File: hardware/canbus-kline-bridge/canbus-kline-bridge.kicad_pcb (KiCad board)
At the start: 4 copper layers, 55 x 35 mm, 38 parts, among them J1 USB_B_Micro, J2 SWD, J4 CANBus, J5 CANBus, J6 K-Line, Q1 2N7002, Q2 2N7002, U1 MCP1754S-3302xCB, U2 STM32F042F6Px, U3 Voltage Regulator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

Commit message: Working on the kline bridge a bit more
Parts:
- removed JP1: CAN_RX/USB_D-, Connector_PinHeader_2.54mm:PinHeader_1x03_P2.54mm_Vertical
- removed JP2: CAN_TX/USB_D+, Connector_PinHeader_2.54mm:PinHeader_1x03_P2.54mm_Vertical
- added R5: 10k, Resistor_SMD:R_0805_2012Metric_Pad1.20x1.40mm_HandSolder, B.Cu at (84.7, 93.2)
- added R6: 10k, Resistor_SMD:R_0805_2012Metric_Pad1.20x1.40mm_HandSolder, B.Cu at (88.1, 91.4)
- added R7: 10k, Resistor_SMD:R_0805_2012Metric_Pad1.20x1.40mm_HandSolder, B.Cu at (75.9, 92.6)
- added R8: 10k, Resistor_SMD:R_0805_2012Metric_Pad1.20x1.40mm_HandSolder, B.Cu at (73.6, 97.0)
- added U6: CY15E004J, Package_SO:SOIC-8_5.23x5.23mm_P1.27mm, B.Cu at (91.6, 86.2)
- added U7: MCP2517FD, Package_SO:SOIC-14_3.9x8.7mm_P1.27mm, F.Cu at (76.0, 96.0)
- added X1: ASV-20.000MHZ-EJ-T, Oscillator:Oscillator_SMD_Abracon_ASV-4Pin_7.0x5.1mm, B.Cu at (68.9, 99.3)
- R3: moved to B.Cu
- moved R1 6.15 mm to (93.0, 96.4), turned to 0 degrees
- moved R2 4.75 mm to (99.9, 93.1)
- moved R3 0.08 mm to (77.4, 87.6)
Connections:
- S1 pad 2: unconnected-(S1-Pad2) -> +3V3
- S1 pad 4: unconnected-(S1-Pad4) -> /Net-(R1-Pad1)
- S2 pad 2: unconnected-(S2-Pad2) -> GND
- S2 pad 4: unconnected-(S2-Pad4) -> ~{RESET}
- U2 pad 10: unconnected-(U2-Pad10) -> ~{SPI_SS}
- U2 pad 11: unconnected-(U2-Pad11) -> SCK
- U2 pad 12: unconnected-(U2-Pad12) -> MISO
- U2 pad 13: unconnected-(U2-Pad13) -> MOSI
- U2 pad 17: Net-(JP1-Pad2) -> USB_D-
- U2 pad 18: Net-(JP2-Pad2) -> USB_D+
- U2 pad 2: SDA1 -> SDA
- U2 pad 3: SCL1 -> SCL
- U2 pad 7: unconnected-(U2-Pad7) -> ~{CAN_INT}
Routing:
- net ~{CAN_INT}: track 0.00 -> 25.5 mm, vias 0 -> 2
- net SCK: track 0.00 -> 18.4 mm, vias 0 -> 2
- net ~{SPI_SS}: track 0.00 -> 18.4 mm, vias 0 -> 2
- net +3V3: track 23.1 -> 40.3 mm, vias 5 -> 11
- net MISO: track 0.00 -> 16.6 mm, vias 0 -> 2
- net MOSI: track 0.00 -> 16.0 mm, vias 0 -> 2
- net Net-(JP1-Pad2): track 13.1 -> 0.00 mm, vias 1 -> 0
- net SCL: track 0.00 -> 9.90 mm, vias 0 -> 2
- net SDA: track 0.00 -> 9.40 mm, vias 0 -> 2
- net USB_D-: track 17.0 -> 25.3 mm, vias 1 -> 2
- net GND: track 18.7 -> 26.6 mm, vias 6 -> 7
- net Net-(JP2-Pad2): track 7.63 -> 0.00 mm, vias 1 -> 0
- net CAN_TX: track 12.5 -> 6.76 mm, vias 1 -> 2
- net Net-(U7-Pad6): track 0.00 -> 4.83 mm, vias 0 -> 1
- net K_LINE_EN: track 17.1 -> 12.8 mm
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
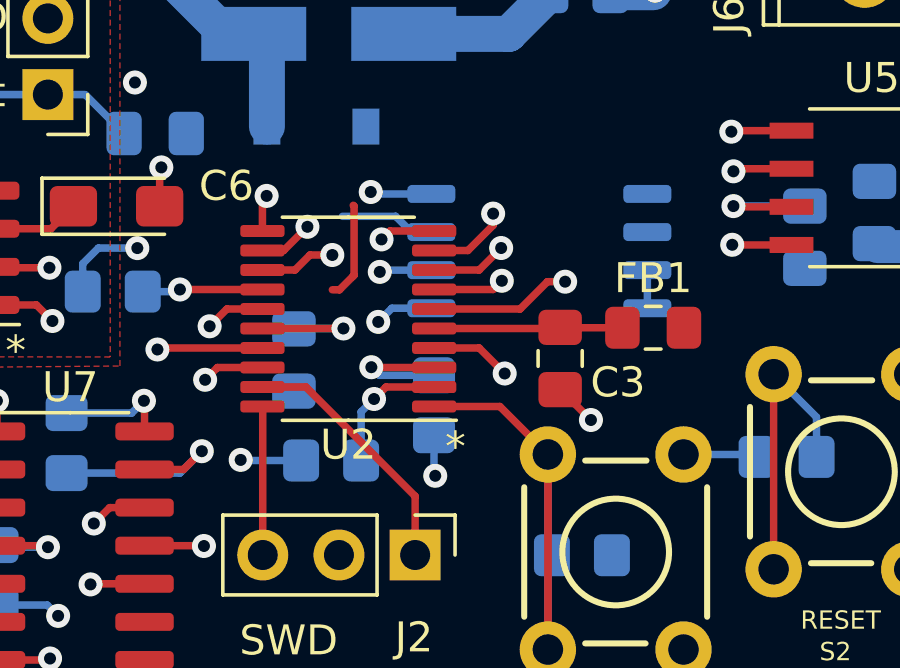
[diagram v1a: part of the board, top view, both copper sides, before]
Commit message: Plumbed out the kline over canbus code
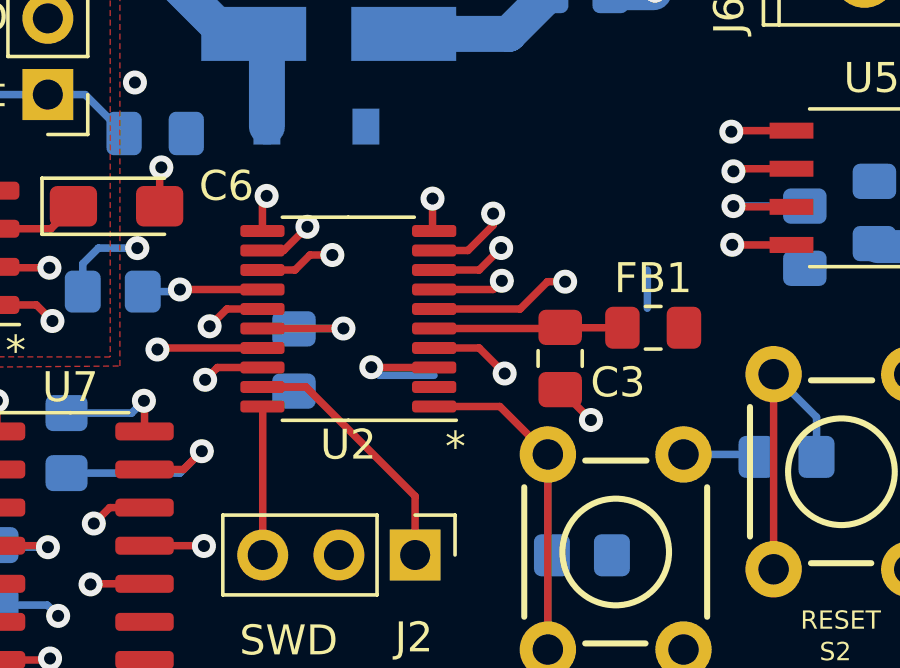
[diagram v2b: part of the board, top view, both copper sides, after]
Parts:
- removed R5, R6: 10k, Resistor_SMD:R_0805_2012Metric_Pad1.20x1.40mm_HandSolder
- removed U6: CY15E004J, Package_SO:SOIC-8_5.23x5.23mm_P1.27mm
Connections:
- U2 pad 2: SDA -> unconnected-(U2-Pad2)
- U2 pad 3: SCL -> unconnected-(U2-Pad3)
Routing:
- net SCL: track 9.90 -> 0.00 mm, vias 2 -> 0
- net SDA: track 9.40 -> 0.00 mm, vias 2 -> 0
- net +3V3: track 40.3 -> 31.6 mm, vias 11 -> 8
- net unconnected-(U2-Pad3): track 0.00 -> 4.30 mm, vias 0 -> 1
- net GND: track 26.6 -> 23.4 mm
- net ~{SPI_SS}: track 18.4 -> 19.7 mm
